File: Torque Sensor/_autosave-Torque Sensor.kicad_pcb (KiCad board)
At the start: 2 copper layers, 33 parts, among them J2 Full Bridge Strain Guage, SW1 SCREW, U2 MCP73831-2-OT, U3 AD7173-8

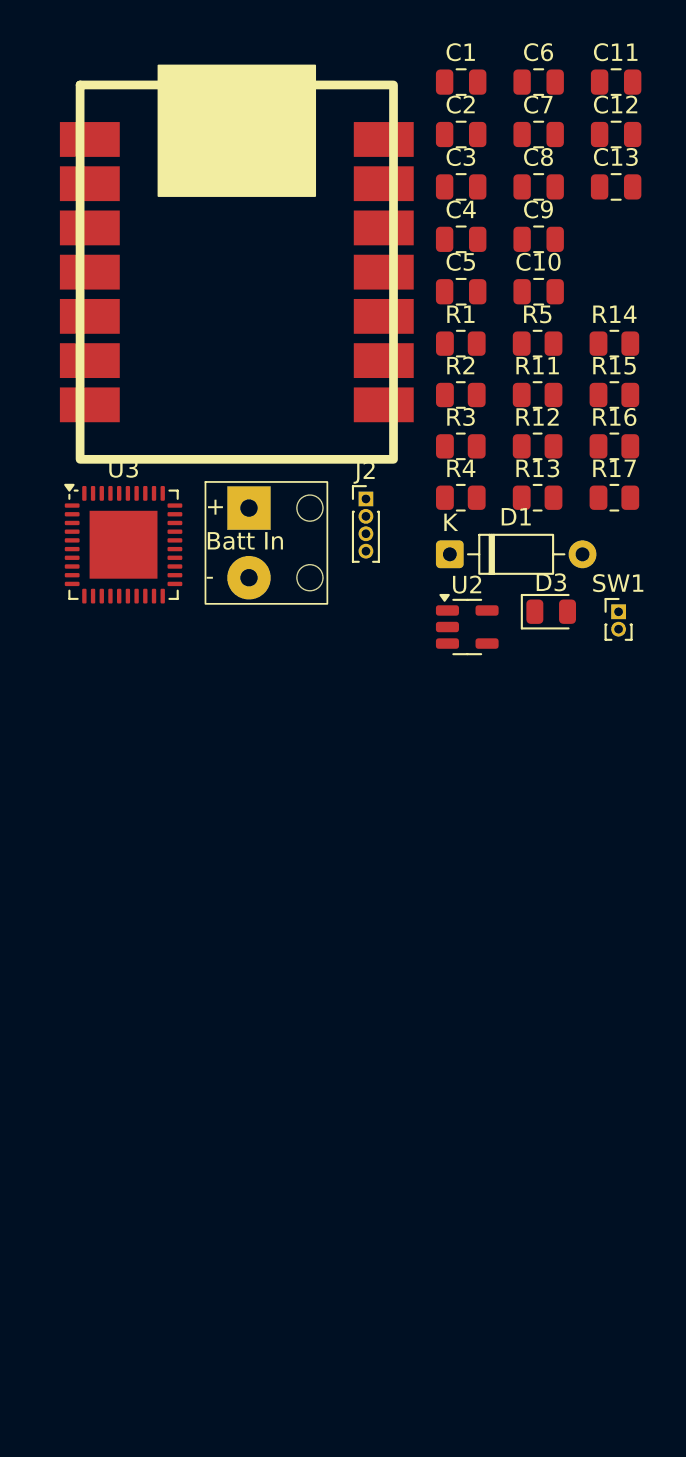
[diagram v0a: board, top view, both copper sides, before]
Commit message: Designed PCB for torque sensor
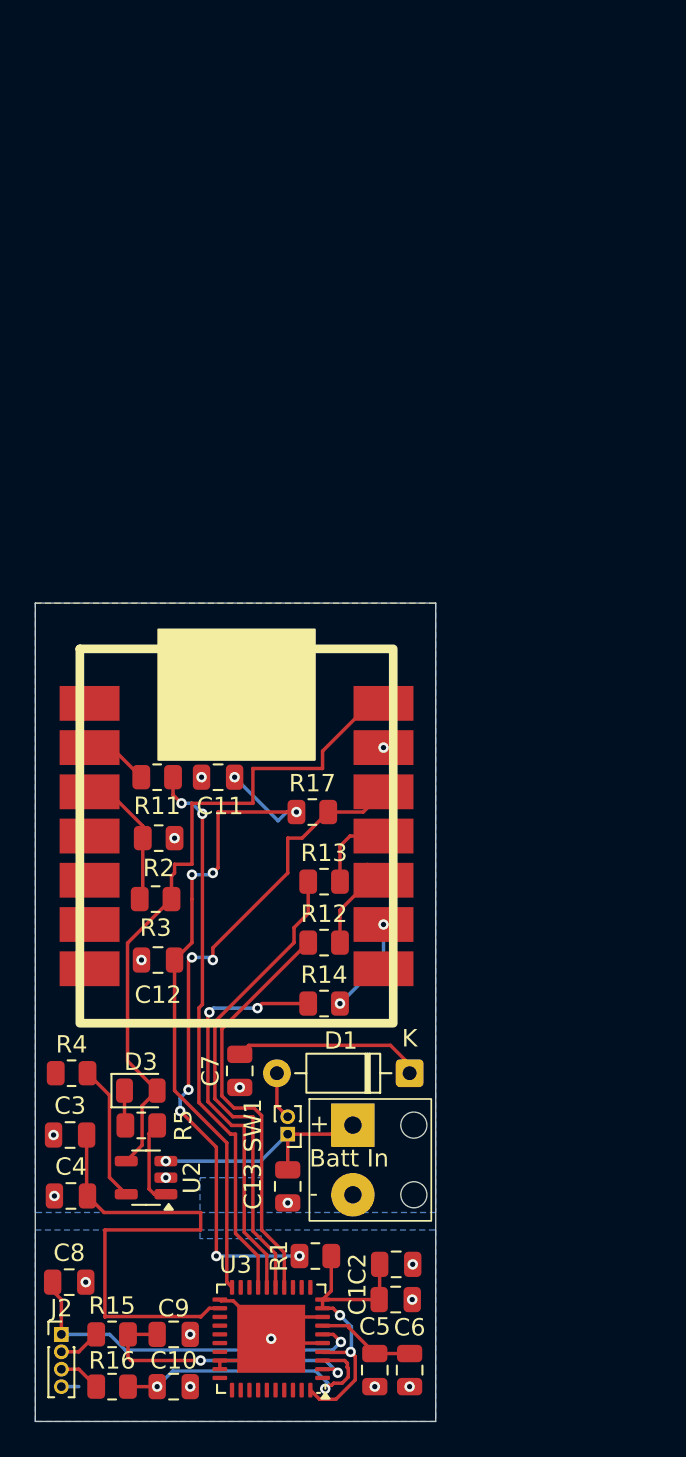
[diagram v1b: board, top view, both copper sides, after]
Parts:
- R5: value 5.1kR -> 1kR
- moved C6 74.3 mm to (141.0, 156.6), turned to 90 degrees
- moved C1 70.0 mm to (140.2, 152.5), turned to 180 degrees
- moved C8 68.4 mm to (121.5, 151.5)
- moved C9 66.3 mm to (127.5, 154.5), turned to 180 degrees
- moved C10 66.3 mm to (127.5, 157.5)
- moved C2 65.0 mm to (140.2, 150.5), turned to 180 degrees
- moved C5 62.1 mm to (139.0, 156.6), turned to 90 degrees
- moved R16 61.2 mm to (123.9, 157.5)
- moved R15 61.2 mm to (123.9, 154.5)
- moved C13 60.4 mm to (134.0, 146.0), turned to -90 degrees
- moved C4 59.3 mm to (121.5, 146.6)
- moved C3 58.9 mm to (121.5, 143.1)
- moved C7 56.4 mm to (131.2, 139.4), turned to 90 degrees
- moved C12 54.2 mm to (126.5, 133.0)
- moved R1 53.1 mm to (135.6, 150.0), turned to 180 degrees
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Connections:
- U3 pad 22: GND -> Net-(U3-REGCAPD)
- U4 pad 2: unconnected-(U4-5V-Pad2) -> +5V
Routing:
- net +5V: track 0.00 -> 49.7 mm
- net +3.3V: track 0.00 -> 41.3 mm, vias 0 -> 6
- net Net-(U3-IOVDD): track 0.00 -> 39.6 mm, vias 0 -> 4
- net Net-(U3-CS): track 0.00 -> 32.0 mm, vias 0 -> 2
- net Net-(U3-REGCAPD): track 0.00 -> 28.7 mm
- net Net-(U3-DIN): track 0.00 -> 27.6 mm
- net Net-(U3-DOUT/RDY): track 0.00 -> 24.0 mm
- net Net-(U3-SCLK): track 0.00 -> 23.5 mm, vias 0 -> 2
- net Net-(J2-Pin_1): track 0.00 -> 21.1 mm, vias 0 -> 1
- net AVDD: track 0.00 -> 19.1 mm, vias 0 -> 2
- net Net-(U3-AIN1/REF2+): track 0.00 -> 16.5 mm, vias 0 -> 2
- net Net-(U3-AIN0/REF2-): track 0.00 -> 16.4 mm, vias 0 -> 2
- net GND: track 0.00 -> 15.4 mm, vias 0 -> 17
- net +BATT: track 0.00 -> 15.1 mm, vias 0 -> 1
- net CHRG_IND: track 0.00 -> 8.14 mm
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- added copper zone on B.Cu, net GND
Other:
- board outline added: 23 x 47 mm
